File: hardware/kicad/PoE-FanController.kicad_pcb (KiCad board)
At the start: 2 copper layers, 70 x 78 mm, 33 parts, among them J2 FAN1, J3 FAN2, J4 FAN3, J5 FAN4, J6 Molex_KK254_3pin, J8 Waveshare_ESP32P4POEETH, U1 LM2587-12

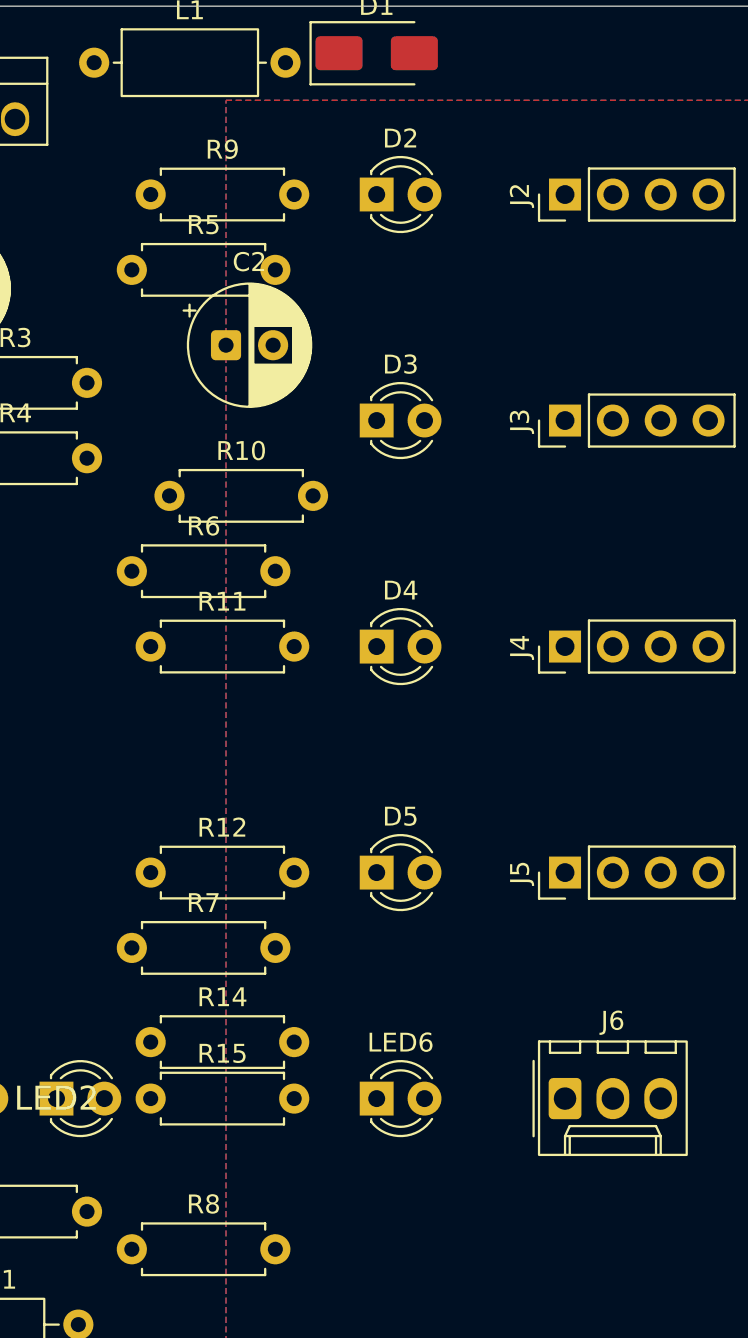
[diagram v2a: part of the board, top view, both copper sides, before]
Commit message: fix(pcb): route DS18B20/LED traces, clean silkscreen, fill zones
- Route DS18B20_DATA: R14 pad2 (43.62,55) -> J6 pad2 (60.54,58) [L-shape]
- Route /PROBE_LED_A: R15 pad2 (43.62,58) -> LED6 pad1 (48.00,58) [horizontal]
- Unconnected items: 73 -> 71 (both new connections resolved)
- Silkscreen: value text hidden for 19 small passives/LEDs
  Reference text repositioned for 20 row-area components
- Zone fill: 2 Net-(U1-GND) copper pours filled
- DRC: 51 violations (34 silk_overlap, 10 silk_over_copper,
  3 silk_edge_clearance, 2 isolated_copper, 1 courtyard, 1 lib)
  All cosmetic — zero electrical violations

Co-authored-by: Copilot <223556219+Copilot@users.noreply.github.com>
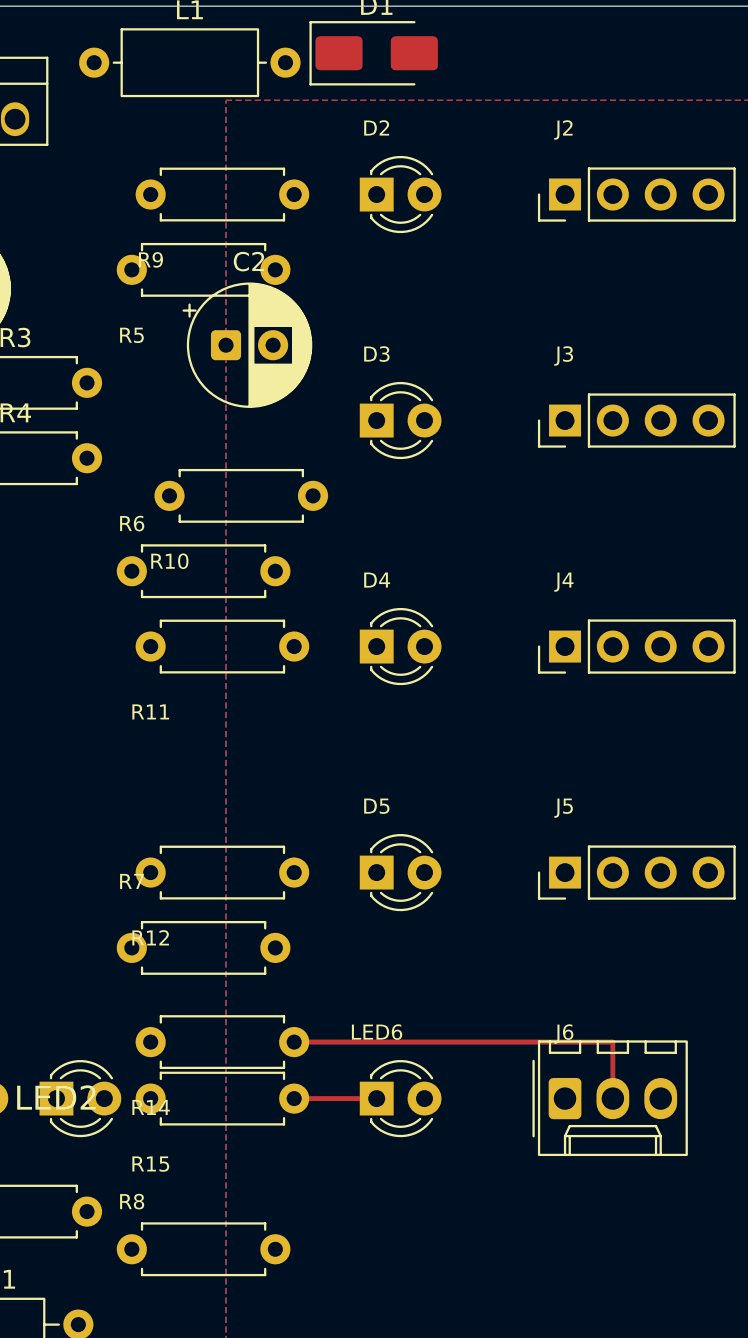
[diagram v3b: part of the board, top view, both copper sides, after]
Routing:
- net DS18B20_DATA: track 0.00 -> 19.9 mm
- net /PROBE_LED_A: track 0.00 -> 4.38 mm
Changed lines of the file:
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@@
 		(tags "Through hole pin header THT 1x04 2.54mm single row")
 		(property "Reference" "J2"
-			(at 0 -2.38 90)
+			(at 3.5 0 0)
 			(layer "F.SilkS")
 			(effects
 				(font
-					(size 1 1)
-					(thickness 0.15)
+					(size 0.8 0.8)
+					(thickness 0.12)
 				)
 			)
@@
 		(tags "Through hole pin header THT 1x04 2.54mm single row")
 		(property "Reference" "J3"
-			(at 0 -2.38 90)
+			(at 3.5 0 0)
 			(layer "F.SilkS")
 			(effects
 				(font
-					(size 1 1)
-					(thickness 0.15)
+					(size 0.8 0.8)
+					(thickness 0.12)
 				)
 			)
@@
 		(tags "Through hole pin header THT 1x04 2.54mm single row")
 		(property "Reference" "J4"
-			(at 0 -2.38 90)
+			(at 3.5 0 0)
 			(layer "F.SilkS")
 			(effects
 				(font
-					(size 1 1)
-					(thickness 0.15)
+					(size 0.8 0.8)
+					(thickness 0.12)
 				)
 			)
@@
 		(tags "Through hole pin header THT 1x04 2.54mm single row")
 		(property "Reference" "J5"
-			(at 0 -2.38 90)
+			(at 3.5 0 0)
 			(layer "F.SilkS")
 			(effects
 				(font
-					(size 1 1)
-					(thickness 0.15)
+					(size 0.8 0.8)
+					(thickness 0.12)
 				)
 			)
@@
 			(at 5.08 2.77 0)
 			(layer "F.Fab")
+			(hide yes)
 			(effects
 				(font
@@
 		(tags "LED")
 		(property "Reference" "D4"
-			(at 1.27 -2.96 0)
+			(at 0 -3.5 0)
 			(layer "F.SilkS")
 			(effects
 				(font
-					(size 1 1)
-					(thickness 0.15)
+					(size 0.8 0.8)
+					(thickness 0.12)
 				)
 			)
@@
 			(at 1.27 2.96 0)
 			(layer "F.Fab")
+			(hide yes)
 			(effects
 				(font
@@
 		(tags "LED")
 		(property "Reference" "D3"
-			(at 1.27 -2.96 0)
+			(at 0 -3.5 0)
 			(layer "F.SilkS")
 			(effects
 				(font
-					(size 1 1)
-					(thickness 0.15)
+					(size 0.8 0.8)
+					(thickness 0.12)
 				)
 			)
@@
 			(at 1.27 2.96 0)
 			(layer "F.Fab")
+			(hide yes)
 			(effects
 				(font
@@
 		(tags "Resistor Axial_DIN0207 series Axial Horizontal pin pitch 7.62mm 0.25W = 1/4W length 6.3mm diameter 2.5mm")
 		(property "Reference" "R8"
-			(at 3.81 -2.37 0)
+			(at 0 -2.5 0)
 			(layer "F.SilkS")
 			(effects
 				(font
-					(size 1 1)
-					(thickness 0.15)
+					(size 0.8 0.8)
+					(thickness 0.12)
 				)
 			)
@@
 			(at 3.81 2.37 0)
 			(layer "F.Fab")
+			(hide yes)
 			(effects
 				(font
@@
 		(tags "Resistor Axial_DIN0207 series Axial Horizontal pin pitch 7.62mm 0.25W = 1/4W length 6.3mm diameter 2.5mm")
 		(property "Reference" "R12"
-			(at 3.81 -2.37 0)
+			(at 0 3.5 0)
 			(layer "F.SilkS")
 			(effects
 				(font
-					(size 1 1)
-					(thickness 0.15)
+					(size 0.8 0.8)
+					(thickness 0.12)
 				)
 			)
@@
 			(at 3.81 2.37 0)
 			(layer "F.Fab")
+			(hide yes)
 			(effects
 				(font
@@
 		(tags "Resistor Axial_DIN0207 series Axial Horizontal pin pitch 7.62mm 0.25W = 1/4W length 6.3mm diameter 2.5mm")
 		(property "Reference" "R11"
-			(at 3.81 -2.37 0)
+			(at 0 3.5 0)
 			(layer "F.SilkS")
 			(effects
 				(font
-					(size 1 1)
-					(thickness 0.15)
+					(size 0.8 0.8)
+					(thickness 0.12)
 				)
 			)
@@
 			(at 3.81 2.37 0)
 			(layer "F.Fab")
+			(hide yes)
 			(effects
 				(font
@@
 		(tags "Resistor Axial_DIN0207 series Axial Horizontal pin pitch 7.62mm 0.25W = 1/4W length 6.3mm diameter 2.5mm")
 		(property "Reference" "R14"
-			(at 3.81 -2.37 0)
+			(at 0 3.5 0)
 			(layer "F.SilkS")
 			(effects
 				(font
-					(size 1 1)
-					(thickness 0.15)
+					(size 0.8 0.8)
+					(thickness 0.12)
 				)
 			)
@@
 			(at 3.81 2.37 0)
 			(layer "F.Fab")
+			(hide yes)
 			(effects
 				(font
@@
 		(tags "Resistor Axial_DIN0207 series Axial Horizontal pin pitch 7.62mm 0.25W = 1/4W length 6.3mm diameter 2.5mm")
 		(property "Reference" "R5"
-			(at 3.81 -2.37 0)
+			(at 0 3.5 0)
 			(layer "F.SilkS")
 			(effects
 				(font
-					(size 1 1)
-					(thickness 0.15)
+					(size 0.8 0.8)
+					(thickness 0.12)
 				)
 			)
@@
 			(at 3.81 2.37 0)
 			(layer "F.Fab")
+			(hide yes)
 			(effects
 				(font
@@
 			(at 1.25 4.4 0)
 			(layer "F.Fab")
+			(hide yes)
 			(effects
 				(font
@@
 		(tags "Resistor Axial_DIN0207 series Axial Horizontal pin pitch 7.62mm 0.25W = 1/4W length 6.3mm diameter 2.5mm")
 		(property "Reference" "R7"
-			(at 3.81 -2.37 0)
+			(at 0 -3.5 0)
 			(layer "F.SilkS")
 			(effects
 				(font
-					(size 1 1)
-					(thickness 0.15)
+					(size 0.8 0.8)
+					(thickness 0.12)
 				)
 			)
@@
 			(at 3.81 2.37 0)
 			(layer "F.Fab")
+			(hide yes)
 			(effects
 				(font
@@
 		(tags "Resistor Axial_DIN0207 series Axial Horizontal pin pitch 7.62mm 0.25W = 1/4W length 6.3mm diameter 2.5mm")
 		(property "Reference" "R6"
-			(at 3.81 -2.37 0)
+			(at 0 -2.5 0)
 			(layer "F.SilkS")
 			(effects
 				(font
-					(size 1 1)
-					(thickness 0.15)
+					(size 0.8 0.8)
+					(thickness 0.12)
 				)
 			)
@@
 			(at 3.81 2.37 0)
 			(layer "F.Fab")
+			(hide yes)
 			(effects
 				(font
@@
 		(tags "Resistor Axial_DIN0207 series Axial Horizontal pin pitch 7.62mm 0.25W = 1/4W length 6.3mm diameter 2.5mm")
 		(property "Reference" "R9"
-			(at 3.81 -2.37 0)
+			(at 0 3.5 0)
 			(layer "F.SilkS")
 			(effects
 				(font
-					(size 1 1)
-					(thickness 0.15)
+					(size 0.8 0.8)
+					(thickness 0.12)
 				)
 			)
@@
 			(at 3.81 2.37 0)
 			(layer "F.Fab")
+			(hide yes)
 			(effects
 				(font
@@
 			(at 1.25 4.4 0)
 			(layer "F.Fab")
+			(hide yes)
 			(effects
 				(font
@@
 		(tags "connector Molex KK-254 vertical")
 		(property "Reference" "J6"
-			(at 2.54 -4.12 0)
+			(at 0 -3.5 0)
 			(layer "F.SilkS")
 			(effects
 				(font
-					(size 1 1)
-					(thickness 0.15)
+					(size 0.8 0.8)
+					(thickness 0.12)
 				)
 			)
@@
 			(at 0 0 0)
 			(layer "F.Fab")
+			(hide yes)
 			(effects
 				(font
@@
 		(tags "Resistor Axial_DIN0207 series Axial Horizontal pin pitch 7.62mm 0.25W = 1/4W length 6.3mm diameter 2.5mm")
 		(property "Reference" "R15"
-			(at 3.81 -2.37 0)
+			(at 0 3.5 0)
 			(layer "F.SilkS")
 			(effects
 				(font
-					(size 1 1)
-					(thickness 0.15)
+					(size 0.8 0.8)
+					(thickness 0.12)
 				)
 			)
@@
 			(at 3.81 2.37 0)
 			(layer "F.Fab")
+			(hide yes)
 			(effects
 				(font
@@
 		(tags "LED")
 		(property "Reference" "D5"
-			(at 1.27 -2.96 0)
+			(at 0 -3.5 0)
 			(layer "F.SilkS")
 			(effects
 				(font
-					(size 1 1)
-					(thickness 0.15)
+					(size 0.8 0.8)
+					(thickness 0.12)
 				)
 			)
@@
 			(at 1.27 2.96 0)
 			(layer "F.Fab")
+			(hide yes)
 			(effects
 				(font
@@
 		(tags "LED")
 		(property "Reference" "D2"
-			(at 1.27 -2.96 0)
+			(at 0 -3.5 0)
 			(layer "F.SilkS")
 			(effects
 				(font
-					(size 1 1)
-					(thickness 0.15)
+					(size 0.8 0.8)
+					(thickness 0.12)
 				)
 			)
@@
 			(at 1.27 2.96 0)
 			(layer "F.Fab")
+			(hide yes)
 			(effects
 				(font
@@
 		(tags "Resistor Axial_DIN0207 series Axial Horizontal pin pitch 7.62mm 0.25W = 1/4W length 6.3mm diameter 2.5mm")
 		(property "Reference" "R10"
-			(at 3.81 -2.37 0)
+			(at 0 3.5 0)
 			(layer "F.SilkS")
 			(effects
 				(font
-					(size 1 1)
-					(thickness 0.15)
+					(size 0.8 0.8)
+					(thickness 0.12)
 				)
 			)
@@
 			(at 3.81 2.37 0)
 			(layer "F.Fab")
+			(hide yes)
 			(effects
 				(font
@@
 		(tags "LED")
 		(property "Reference" "LED6"
-			(at 1.27 -2.96 0)
+			(at 0 -3.5 0)
 			(layer "F.SilkS")
 			(effects
 				(font
-					(size 1 1)
-					(thickness 0.15)
+					(size 0.8 0.8)
+					(thickness 0.12)
 				)
 			)
@@
 			(at 1.27 2.96 0)
 			(layer "F.Fab")
+			(hide yes)
 			(effects
 				(font
@@
 		)
 	)
+	(segment
+		(start 60.54 55)
+		(end 60.54 58)
+		(width 0.25)
+		(layer "F.Cu")
+		(net "DS18B20_DATA")
+	)
+	(segment
+		(start 43.62 55)
+		(end 60.54 55)
+		(width 0.25)
+		(layer "F.Cu")
+		(net "DS18B20_DATA")
+	)
+	(segment
+		(start 43.62 58)
+		(end 48 58)
+		(width 0.25)
+		(layer "F.Cu")
+		(net "/PROBE_LED_A")
+	)
 	(zone

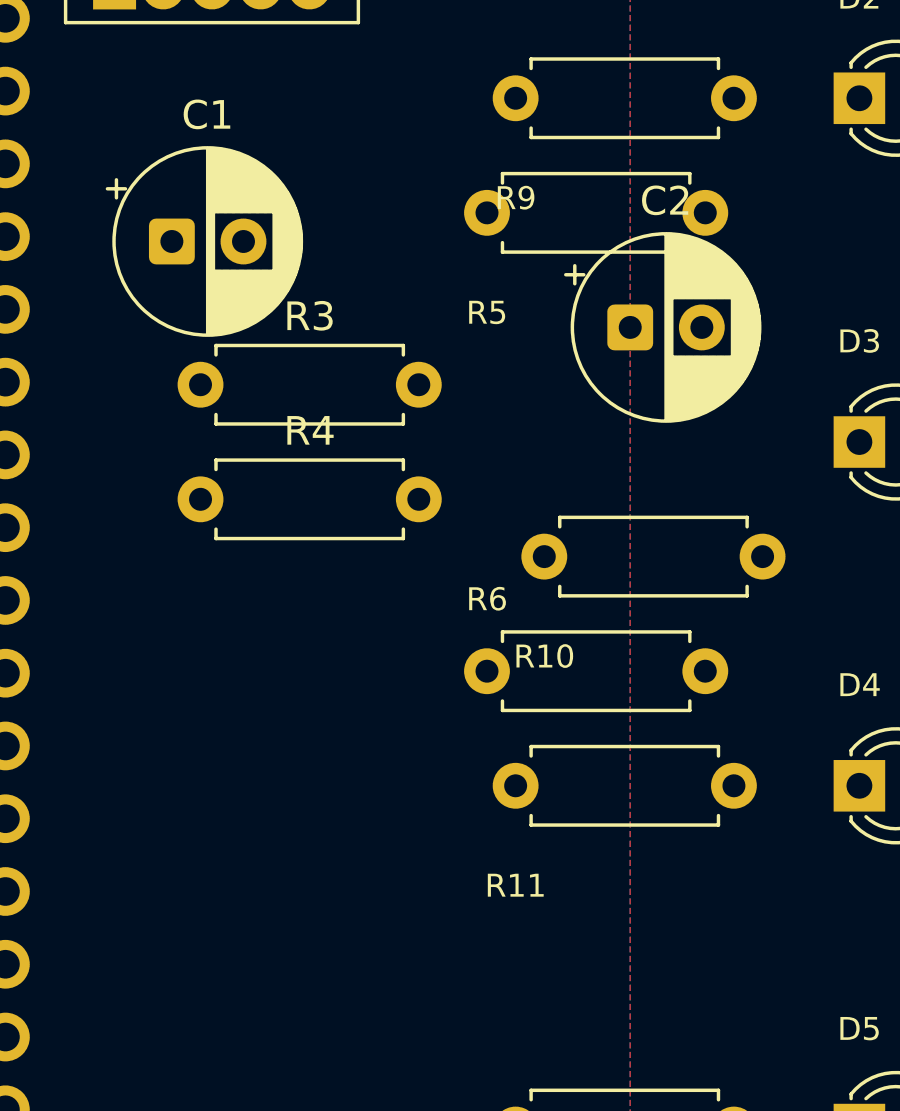
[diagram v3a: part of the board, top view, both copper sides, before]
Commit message: fix(pcb): move R5 to (25,35) to eliminate courtyard error
R5 at (35,14) had courtyard overlap with C2 (100uF power cap at 40,18)
which was severity=error and failed CI Hardware Check.

New position (25,35) verified clear of all neighbouring courtyards:
C1, C2, R3, R4, R6, R7, R9, R10, R11, J8, LED1.

DRC: 16 violations (0 errors), 71 unconnected.

Co-authored-by: Copilot <223556219+Copilot@users.noreply.github.com>
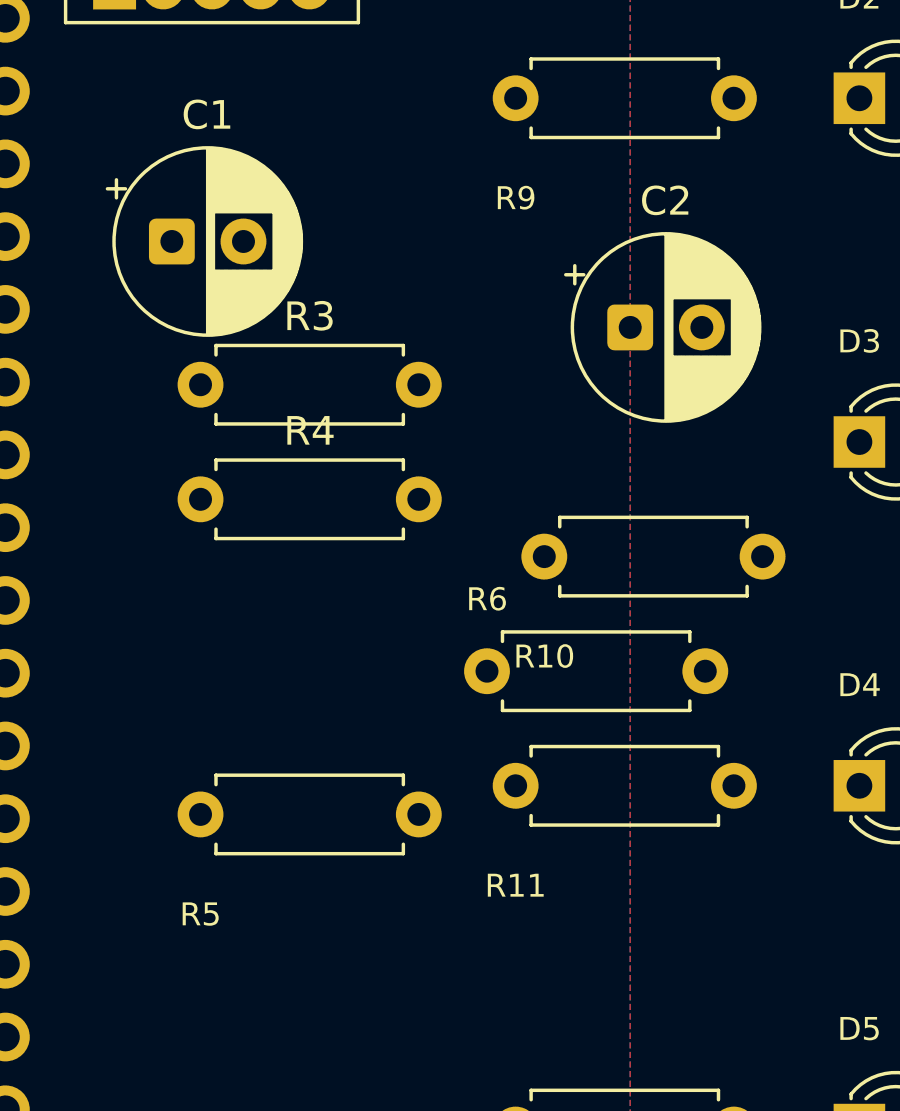
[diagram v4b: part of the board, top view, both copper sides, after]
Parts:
- moved R5 23.3 mm to (25.0, 35.0)
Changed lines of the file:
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@@
 	(footprint "R_Axial_DIN0207_L6.3mm_D2.5mm_P7.62mm_Horizontal"
 		(layer "F.Cu")
-		(at 35 14)
+		(at 25 35)
 		(descr "Resistor, Axial_DIN0207 series, Axial, Horizontal, pin pitch=7.62mm, 0.25W = 1/4W, length*diameter=6.3*2.5mm^2, http://cdn-reichelt.de/documents/datenblatt/B400/1_4W%23YAG.pdf")
 		(tags "Resistor Axial_DIN0207 series Axial Horizontal pin pitch 7.62mm 0.25W = 1/4W length 6.3mm diameter 2.5mm")

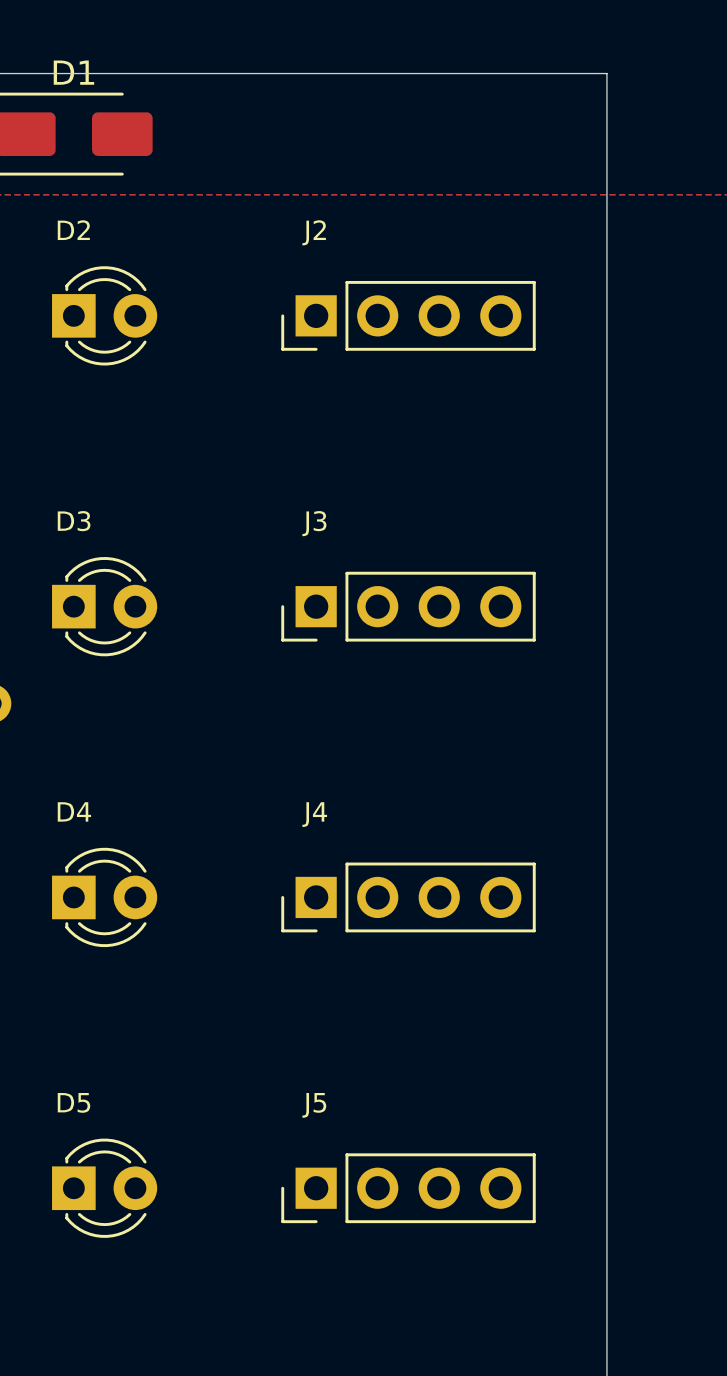
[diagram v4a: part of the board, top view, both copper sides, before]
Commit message: hw(#100): swap J2-J5 PCB footprints to Molex KK-254 and re-place connectors
- T005: replaced J2-J5 footprints from PinHeader_1x04 to
  Connector_Molex:Molex_KK-254_AE-6410-04A_1x04_P2.54mm_Vertical
  via pcbnew Python API; net assignments preserved (GND/+12V/TACH/PWM)
- T005: positions confirmed: J2(58,10) J3(58,22) J4(58,34) J5(58,46)
  all at rotation 90deg; shroud key toward +X board edge
- T005: copper zones refilled after footprint swap
- T006: DRC passes - 0 errors, 0 courtyard_collision, 16 warnings, 71 ratsnest

Refs #124
Refs #125

Co-authored-by: Copilot <223556219+Copilot@users.noreply.github.com>
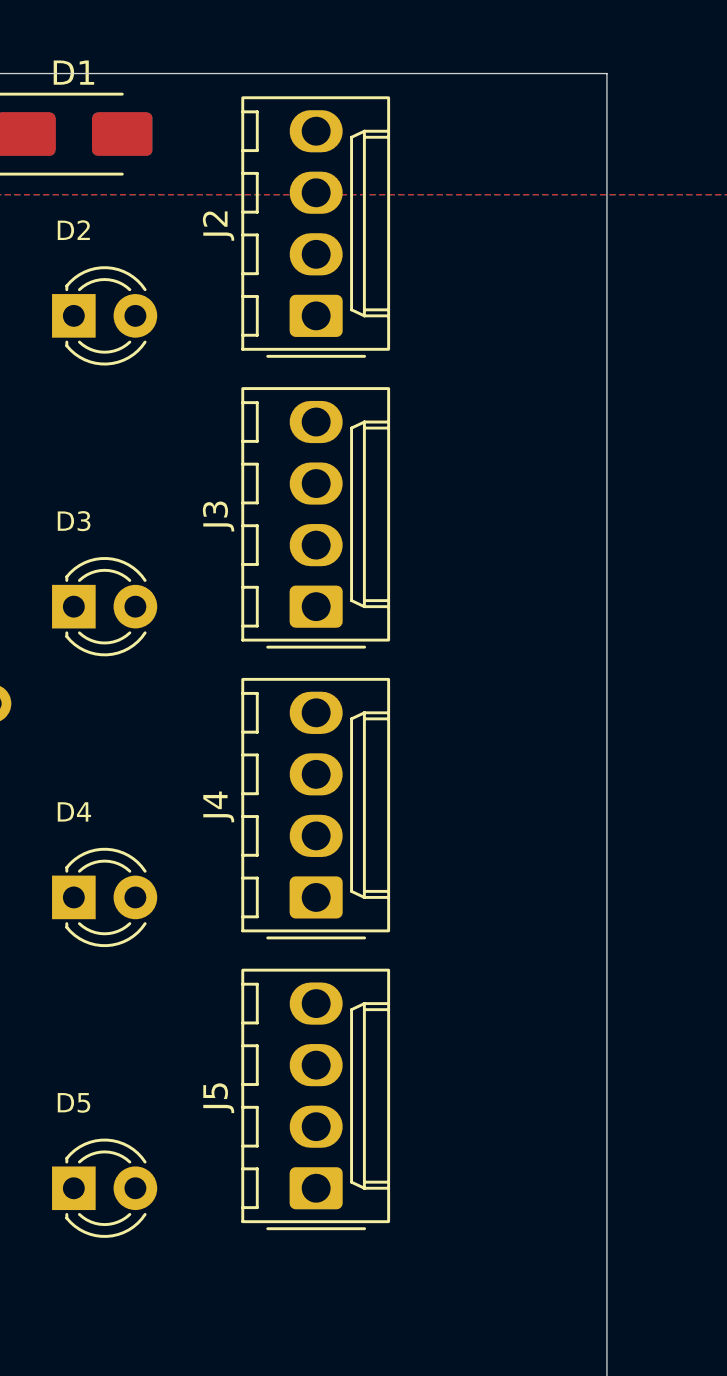
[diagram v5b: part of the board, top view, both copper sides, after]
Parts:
- J2, J3, J4, J5: footprint Connector_PinHeader_2.54mm:PinHeader_1x04_P2.54mm_Vertical -> Connector_Molex:Molex_KK-254_AE-6410-04A_1x04_P2.54mm_Vertical
